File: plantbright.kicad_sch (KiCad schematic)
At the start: 24 parts, among them J1 POWER OUT, J2 SPEAKER, J4 5V IN, Q1 AO3400A, Q2 AO3400A, Q3 AO3400A, Q4 AO3400A, Q5 AO3400A, SW1 USER 0, SW2 USER 1, U1 XIAO-ESP32-C6, U2 DFPLAYER MINI

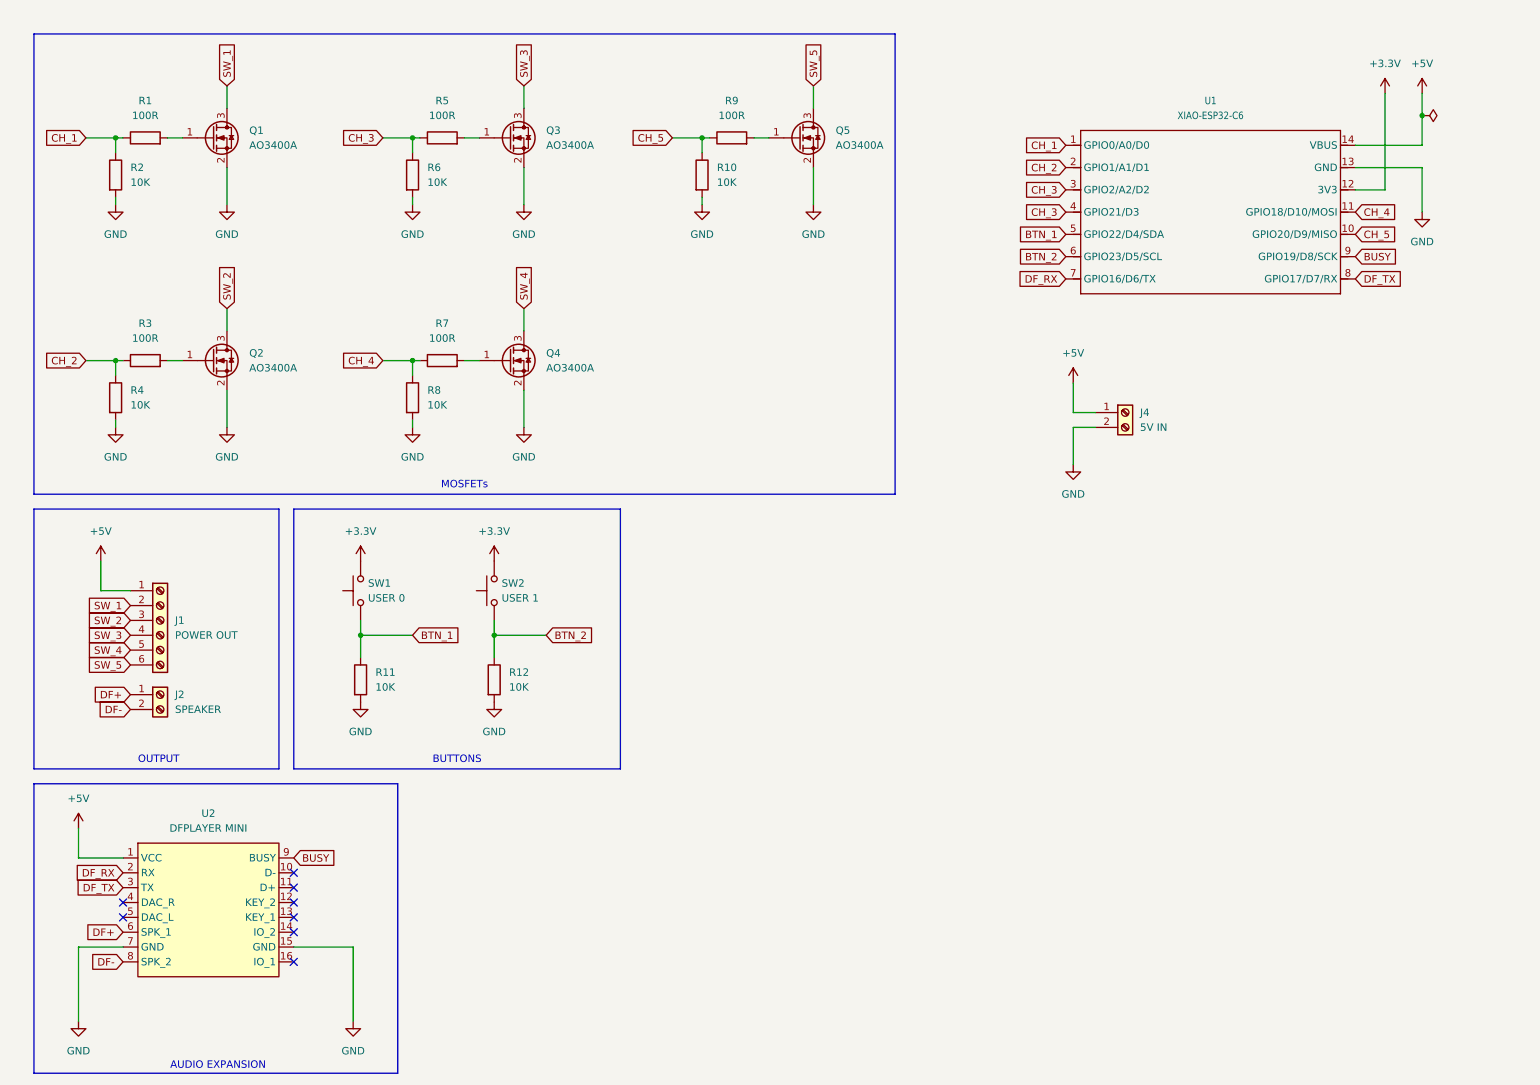
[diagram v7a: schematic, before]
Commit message: Remove dfplayer.
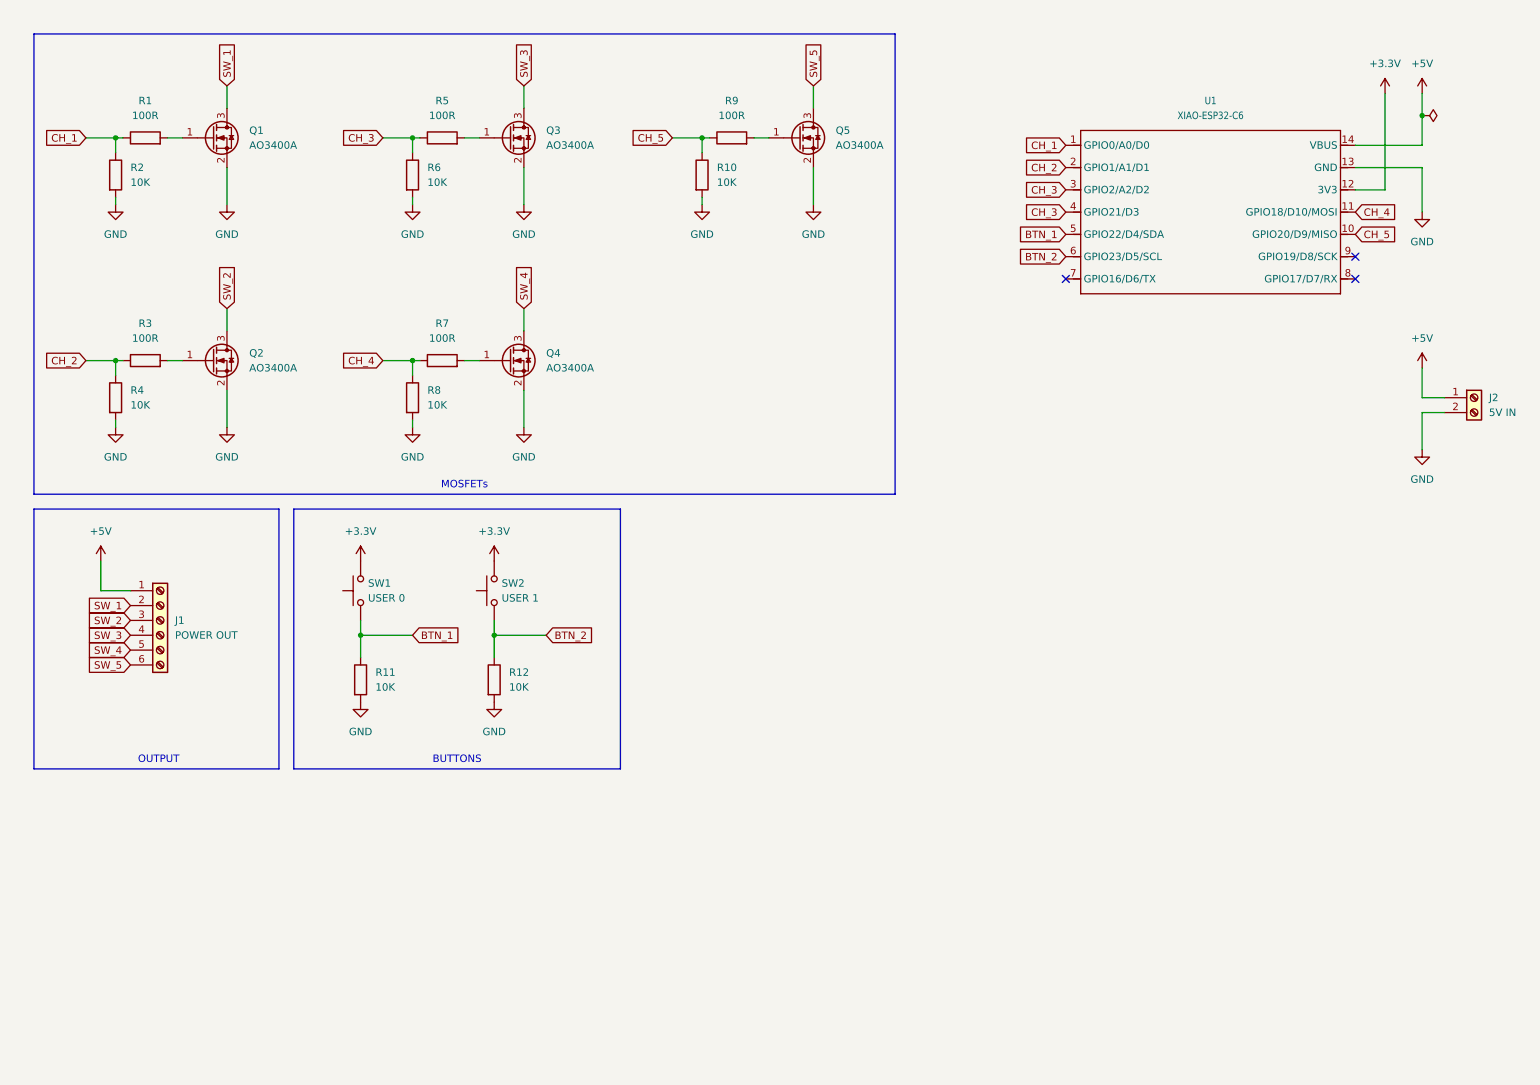
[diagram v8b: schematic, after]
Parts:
- removed J2: SPEAKER, Connector_JST:JST_XH_B2B-XH-A_1x02_P2.50mm_Vertical, symbol Connector:Screw_Terminal_01x02
- removed U2: DFPLAYER MINI, kicad-dfplayermini:dfplayer, symbol dfplayer:DFPlayerMini
- renumbered J4 to J2
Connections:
- net BUSY: no longer names the net of U1.9 (GPIO19/D8/SCK)
- net DF_RX: no longer names the net of U1.7 (GPIO16/D6/TX)
- net DF_TX: no longer names the net of U1.8 (GPIO17/D7/RX)
- no-connect marks 8 -> 3
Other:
- note removed: "AUDIO EXPANSION"
- moved on the sheet: J2
